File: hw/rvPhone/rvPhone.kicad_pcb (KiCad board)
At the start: 4 copper layers, 126 x 68 mm, 262 parts, among them J1 USB_OTG, J2 BATT, J201 Modem, J202 SIM_Card, J203 Motor, J204 Micro_SD_Card_Det, J205 Prog, J206 Expansion, J207 Camera, J3 +5V, J301 iMX8, J302 Micro_SD_Card_Det, J303 Spacer, J4 SJ-3571N, J401 Display, J402 Spacer, J403 Spacer, J5 SPEAKER, SW1 RESET, SW2 WAKE, SW201 ESP32_RST, SW202 MODEM_RST, SW301 iMX8_ALT_BOOT, SW302 iMX8_RST, SW303 iMX8_PWR, U1 BQ25895, U10 74HC595, U11 ICS-43434, U12 MAX98357A, U13 MAX98357A, U14 SN74LVC1G04DCK, U15 SN74LVC1G3157DCK, U16 SN74LVC2G07DCK, U2 TPS62293, U201 ESP32-WROOM, U202 SN74CBTLV3125RGY, U203 TXB0104RGY, U204 TXB0104RGY, U205 DRV2605LDGS, U206 LSM9DS1, U207 FT230XQ, U208 TMUX154ERSW, U3 TPS630250, U4 FE310-G002, U401 FAN5333BSX, U402 SN74LVC3G06DCU, U403 BT817Q, U404 IS25LP128-JKLE, U405 DS90C185, U406 TS3DV520ERUA, U407 TMUX1574RSV, U5 IS25LP128-JKLE, U6 TMUX1574RSV, U7 74HC00, U8 74HC00, U9 74HC595, X1 SiT1533, Y1 16MHz, Y401 12MHz

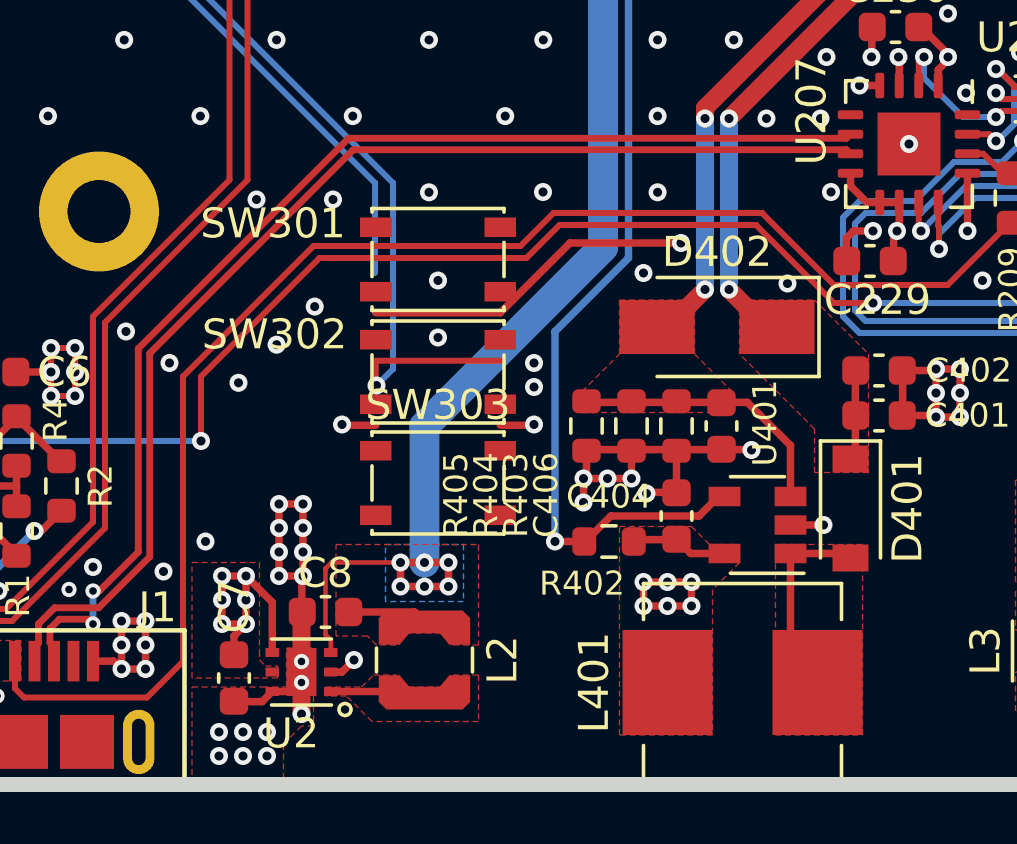
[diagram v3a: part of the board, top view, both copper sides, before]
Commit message: added missing components/footprints
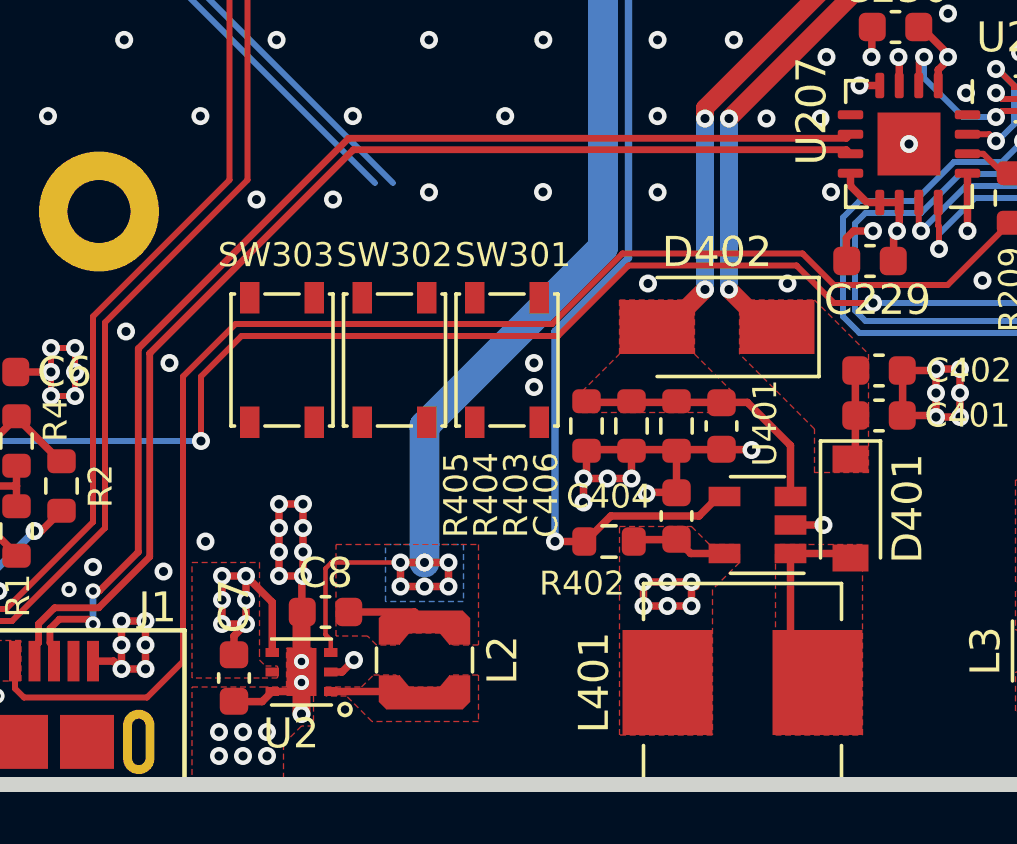
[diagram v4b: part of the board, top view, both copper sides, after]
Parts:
- moved SW303 6.62 mm to (126.5, 125.8), turned to 90 degrees
- moved SW301 4.06 mm to (134.0, 125.8), turned to 90 degrees
- moved SW302 1.50 mm to (130.2, 125.8), turned to 90 degrees
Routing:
- net /exp/RESET: track 73.1 -> 61.1 mm, vias 2 -> 1
- net +3V3: track 244.1 -> 232.9 mm, vias 78 -> 77
- net /exp/ALT_BOOT: track 60.4 -> 57.4 mm
- net GND: track 505.2 -> 502.9 mm, vias 639 -> 632
- net /BQ_QON: track 93.0 -> 91.9 mm
- net VBUS: track 48.4 -> 47.2 mm
